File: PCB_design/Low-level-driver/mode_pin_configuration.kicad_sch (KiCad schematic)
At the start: 12 parts, among them Q301 BC846BPN, Q302 Q_NPN_EBC, Q303 Q_NPN_EBC, Q304 Q_NPN_EBC, U301 TMUX1204DQAR

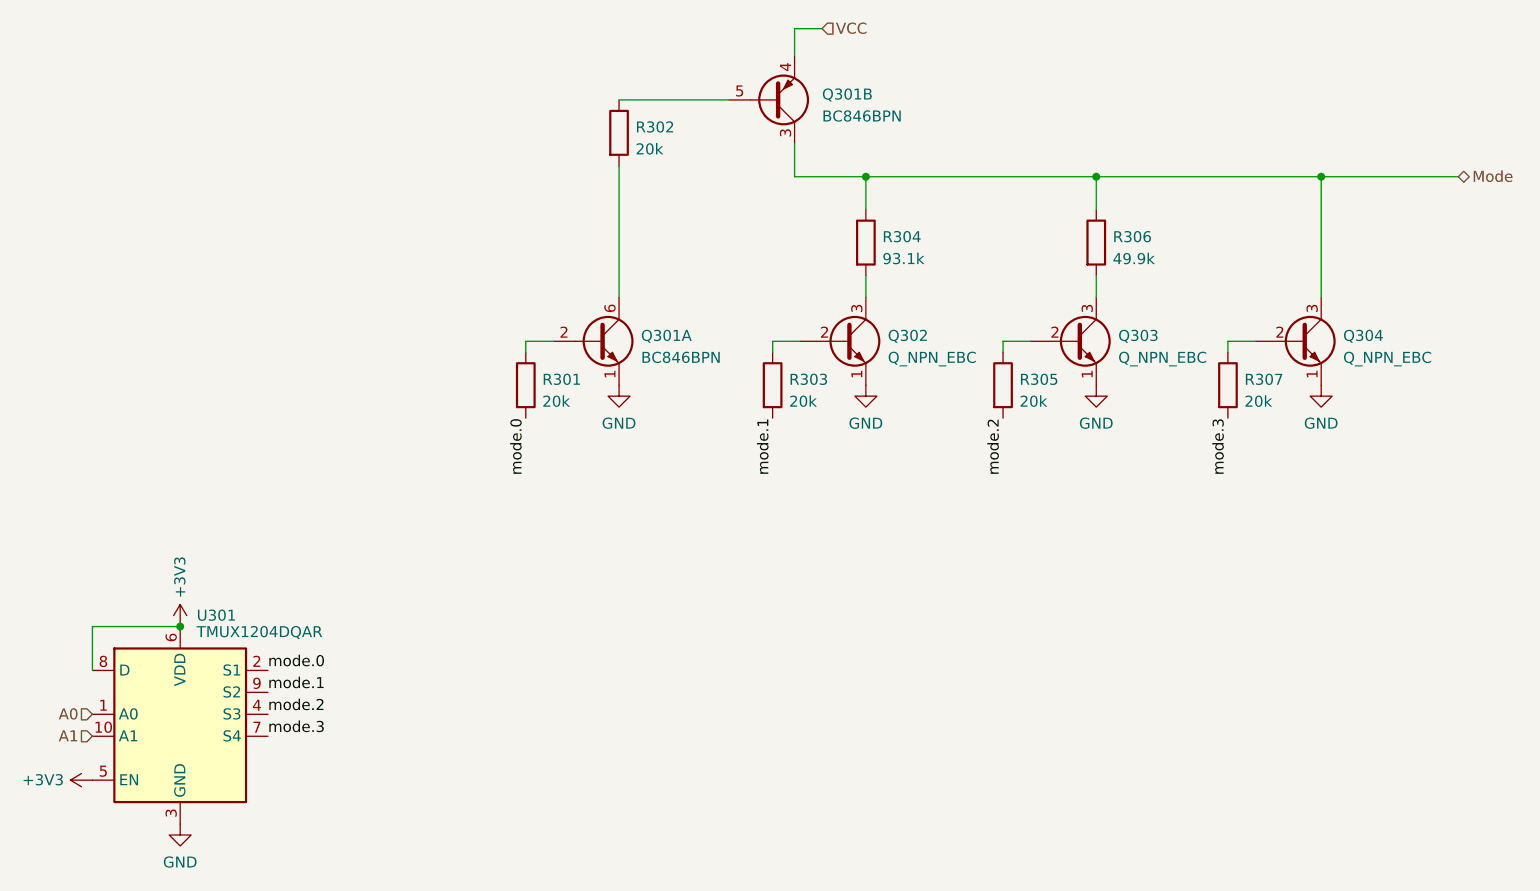
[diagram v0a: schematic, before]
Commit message: Schematic hierarchical redesign
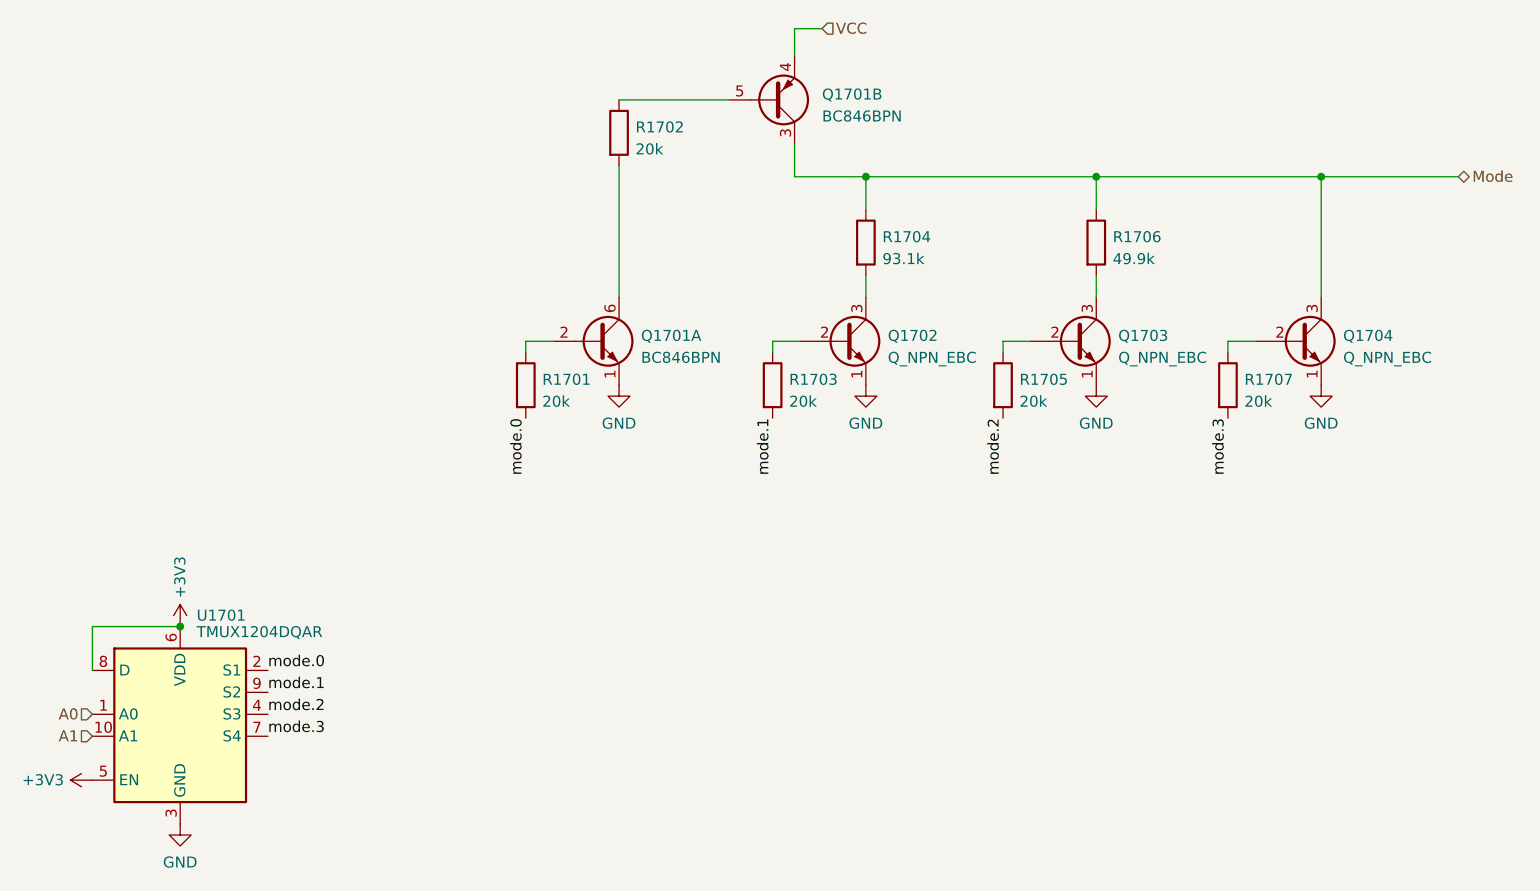
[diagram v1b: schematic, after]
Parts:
- renumbered Q301 to Q1701, Q302 to Q1702, Q303 to Q1703, Q304 to Q1704, R301 to R1701, R302 to R1702, R303 to R1703, R304 to R1704, R305 to R1705, R306 to R1706, R307 to R1707, U301 to U1701
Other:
- title: (none) -> Power supply - low level driver
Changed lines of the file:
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@@
 	(generator_version "8.0")
 	(paper "A3")
+	(title_block
+		(title "Power supply - low level driver")
+		(date "2024-06-28")
+	)
 	(junction
 		(at 179.705 68.58)
@@
 		(on_board yes)
 		(dnp no)
-		(property "Reference" "Q301"
+		(property "Reference" "Q1701"
 			(at 147.955 59.055 0)
 			(effects
@@
 			(project "Low-level-driver"
 				(path "/2e43a8c9-1b23-4896-a481-133b23afb346/01ca3785-0e3e-4a04-8db2-6c3c91b7e708/8ab1ebaa-6c81-454c-95da-69d323116c23"
-					(reference "Q301")
+					(reference "Q1701")
 					(unit 2)
 				)
@@
 		(dnp no)
 		(fields_autoplaced yes)
-		(property "Reference" "R302"
+		(property "Reference" "R1702"
 			(at 126.365 62.865 0)
 			(effects
@@
 			(project "Low-level-driver"
 				(path "/2e43a8c9-1b23-4896-a481-133b23afb346/01ca3785-0e3e-4a04-8db2-6c3c91b7e708/8ab1ebaa-6c81-454c-95da-69d323116c23"
-					(reference "R302")
+					(reference "R1702")
 					(unit 1)
 				)
@@
 		(dnp no)
 		(fields_autoplaced yes)
-		(property "Reference" "R305"
+		(property "Reference" "R1705"
 			(at 170.815 92.075 0)
 			(effects
@@
 			(project "Low-level-driver"
 				(path "/2e43a8c9-1b23-4896-a481-133b23afb346/01ca3785-0e3e-4a04-8db2-6c3c91b7e708/8ab1ebaa-6c81-454c-95da-69d323116c23"
-					(reference "R305")
+					(reference "R1705")
 					(unit 1)
 				)
@@
 		(dnp no)
 		(fields_autoplaced yes)
-		(property "Reference" "U301"
+		(property "Reference" "U1701"
 			(at 75.565 119.38 0)
 			(effects
@@
 			(project "Low-level-driver"
 				(path "/2e43a8c9-1b23-4896-a481-133b23afb346/01ca3785-0e3e-4a04-8db2-6c3c91b7e708/8ab1ebaa-6c81-454c-95da-69d323116c23"
-					(reference "U301")
+					(reference "U1701")
 					(unit 1)
 				)
@@
 		(dnp no)
 		(fields_autoplaced yes)
-		(property "Reference" "#PWR0304"
+		(property "Reference" "#PWR01704"
 			(at 124.46 99.06 0)
 			(effects
@@
 			(project "Low-level-driver"
 				(path "/2e43a8c9-1b23-4896-a481-133b23afb346/01ca3785-0e3e-4a04-8db2-6c3c91b7e708/8ab1ebaa-6c81-454c-95da-69d323116c23"
-					(reference "#PWR0304")
+					(reference "#PWR01704")
 					(unit 1)
 				)
@@
 		(dnp no)
 		(fields_autoplaced yes)
-		(property "Reference" "#PWR0305"
+		(property "Reference" "#PWR01705"
 			(at 153.035 99.06 0)
 			(effects
@@
 			(project "Low-level-driver"
 				(path "/2e43a8c9-1b23-4896-a481-133b23afb346/01ca3785-0e3e-4a04-8db2-6c3c91b7e708/8ab1ebaa-6c81-454c-95da-69d323116c23"
-					(reference "#PWR0305")
+					(reference "#PWR01705")
 					(unit 1)
 				)
@@
 		(dnp no)
 		(fields_autoplaced yes)
-		(property "Reference" "Q304"
+		(property "Reference" "Q1704"
 			(at 208.28 86.995 0)
 			(effects
@@
 			(project "Low-level-driver"
 				(path "/2e43a8c9-1b23-4896-a481-133b23afb346/01ca3785-0e3e-4a04-8db2-6c3c91b7e708/8ab1ebaa-6c81-454c-95da-69d323116c23"
-					(reference "Q304")
+					(reference "Q1704")
 					(unit 1)
 				)
@@
 		(dnp no)
 		(fields_autoplaced yes)
-		(property "Reference" "R306"
+		(property "Reference" "R1706"
 			(at 181.61 75.565 0)
 			(effects
@@
 			(project "Low-level-driver"
 				(path "/2e43a8c9-1b23-4896-a481-133b23afb346/01ca3785-0e3e-4a04-8db2-6c3c91b7e708/8ab1ebaa-6c81-454c-95da-69d323116c23"
-					(reference "R306")
+					(reference "R1706")
 					(unit 1)
 				)
@@
 		(on_board yes)
 		(dnp no)
-		(property "Reference" "#PWR0301"
+		(property "Reference" "#PWR01701"
 			(at 67.31 138.43 0)
 			(effects
@@
 			(project "Low-level-driver"
 				(path "/2e43a8c9-1b23-4896-a481-133b23afb346/01ca3785-0e3e-4a04-8db2-6c3c91b7e708/8ab1ebaa-6c81-454c-95da-69d323116c23"
-					(reference "#PWR0301")
+					(reference "#PWR01701")
 					(unit 1)
 				)
@@
 		(on_board yes)
 		(dnp no)
-		(property "Reference" "Q301"
+		(property "Reference" "Q1701"
 			(at 127 86.995 0)
 			(effects
@@
 			(project "Low-level-driver"
 				(path "/2e43a8c9-1b23-4896-a481-133b23afb346/01ca3785-0e3e-4a04-8db2-6c3c91b7e708/8ab1ebaa-6c81-454c-95da-69d323116c23"
-					(reference "Q301")
+					(reference "Q1701")
 					(unit 1)
 				)
@@
 		(dnp no)
 		(fields_autoplaced yes)
-		(property "Reference" "#PWR0307"
+		(property "Reference" "#PWR01707"
 			(at 205.74 99.06 0)
 			(effects
@@
 			(project "Low-level-driver"
 				(path "/2e43a8c9-1b23-4896-a481-133b23afb346/01ca3785-0e3e-4a04-8db2-6c3c91b7e708/8ab1ebaa-6c81-454c-95da-69d323116c23"
-					(reference "#PWR0307")
+					(reference "#PWR01707")
 					(unit 1)
 				)
@@
 		(dnp no)
 		(fields_autoplaced yes)
-		(property "Reference" "Q302"
+		(property "Reference" "Q1702"
 			(at 155.575 86.995 0)
 			(effects
@@
 			(project "Low-level-driver"
 				(path "/2e43a8c9-1b23-4896-a481-133b23afb346/01ca3785-0e3e-4a04-8db2-6c3c91b7e708/8ab1ebaa-6c81-454c-95da-69d323116c23"
-					(reference "Q302")
+					(reference "Q1702")
 					(unit 1)
 				)
@@
 		(dnp no)
 		(fields_autoplaced yes)
-		(property "Reference" "R304"
+		(property "Reference" "R1704"
 			(at 154.94 75.565 0)
 			(effects
@@
 			(project "Low-level-driver"
 				(path "/2e43a8c9-1b23-4896-a481-133b23afb346/01ca3785-0e3e-4a04-8db2-6c3c91b7e708/8ab1ebaa-6c81-454c-95da-69d323116c23"
-					(reference "R304")
+					(reference "R1704")
 					(unit 1)
 				)
@@
 		(dnp no)
 		(fields_autoplaced yes)
-		(property "Reference" "#PWR0306"
+		(property "Reference" "#PWR01706"
 			(at 179.705 99.06 0)
 			(effects
@@
 			(project "Low-level-driver"
 				(path "/2e43a8c9-1b23-4896-a481-133b23afb346/01ca3785-0e3e-4a04-8db2-6c3c91b7e708/8ab1ebaa-6c81-454c-95da-69d323116c23"
-					(reference "#PWR0306")
+					(reference "#PWR01706")
 					(unit 1)
 				)
@@
 		(dnp no)
 		(fields_autoplaced yes)
-		(property "Reference" "R301"
+		(property "Reference" "R1701"
 			(at 115.57 92.075 0)
 			(effects
@@
 			(project "Low-level-driver"
 				(path "/2e43a8c9-1b23-4896-a481-133b23afb346/01ca3785-0e3e-4a04-8db2-6c3c91b7e708/8ab1ebaa-6c81-454c-95da-69d323116c23"
-					(reference "R301")
+					(reference "R1701")
 					(unit 1)
 				)
@@
 		(dnp no)
 		(fields_autoplaced yes)
-		(property "Reference" "R307"
+		(property "Reference" "R1707"
 			(at 196.85 92.075 0)
 			(effects
@@
 			(project "Low-level-driver"
 				(path "/2e43a8c9-1b23-4896-a481-133b23afb346/01ca3785-0e3e-4a04-8db2-6c3c91b7e708/8ab1ebaa-6c81-454c-95da-69d323116c23"
-					(reference "R307")
+					(reference "R1707")
 					(unit 1)
 				)
@@
 		(on_board yes)
 		(dnp no)
-		(property "Reference" "#PWR0302"
+		(property "Reference" "#PWR01702"
 			(at 73.66 124.46 0)
 			(effects
@@
 			(project "Low-level-driver"
 				(path "/2e43a8c9-1b23-4896-a481-133b23afb346/01ca3785-0e3e-4a04-8db2-6c3c91b7e708/8ab1ebaa-6c81-454c-95da-69d323116c23"
-					(reference "#PWR0302")
+					(reference "#PWR01702")
 					(unit 1)
 				)
@@
 		(dnp no)
 		(fields_autoplaced yes)
-		(property "Reference" "Q303"
+		(property "Reference" "Q1703"
 			(at 182.245 86.995 0)
 			(effects
@@
 			(project "Low-level-driver"
 				(path "/2e43a8c9-1b23-4896-a481-133b23afb346/01ca3785-0e3e-4a04-8db2-6c3c91b7e708/8ab1ebaa-6c81-454c-95da-69d323116c23"
-					(reference "Q303")
+					(reference "Q1703")
 					(unit 1)
 				)
@@
 		(dnp no)
 		(fields_autoplaced yes)
-		(property "Reference" "#PWR0303"
+		(property "Reference" "#PWR01703"
 			(at 73.66 149.86 0)
 			(effects
@@
 			(project "Low-level-driver"
 				(path "/2e43a8c9-1b23-4896-a481-133b23afb346/01ca3785-0e3e-4a04-8db2-6c3c91b7e708/8ab1ebaa-6c81-454c-95da-69d323116c23"
-					(reference "#PWR0303")
+					(reference "#PWR01703")
 					(unit 1)
 				)
@@
 		(dnp no)
 		(fields_autoplaced yes)
-		(property "Reference" "R303"
+		(property "Reference" "R1703"
 			(at 144.145 92.075 0)
 			(effects
@@
 			(project "Low-level-driver"
 				(path "/2e43a8c9-1b23-4896-a481-133b23afb346/01ca3785-0e3e-4a04-8db2-6c3c91b7e708/8ab1ebaa-6c81-454c-95da-69d323116c23"
-					(reference "R303")
-					(unit 1)
-				)
+					(reference "R1703")
+					(unit 1)
+				)
